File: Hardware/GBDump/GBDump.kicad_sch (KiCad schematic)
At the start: 5 parts, among them U2 TXB0108PW, U3 TXB0108PW, U4 TXB0108PW, U5 Cartridge_Bus

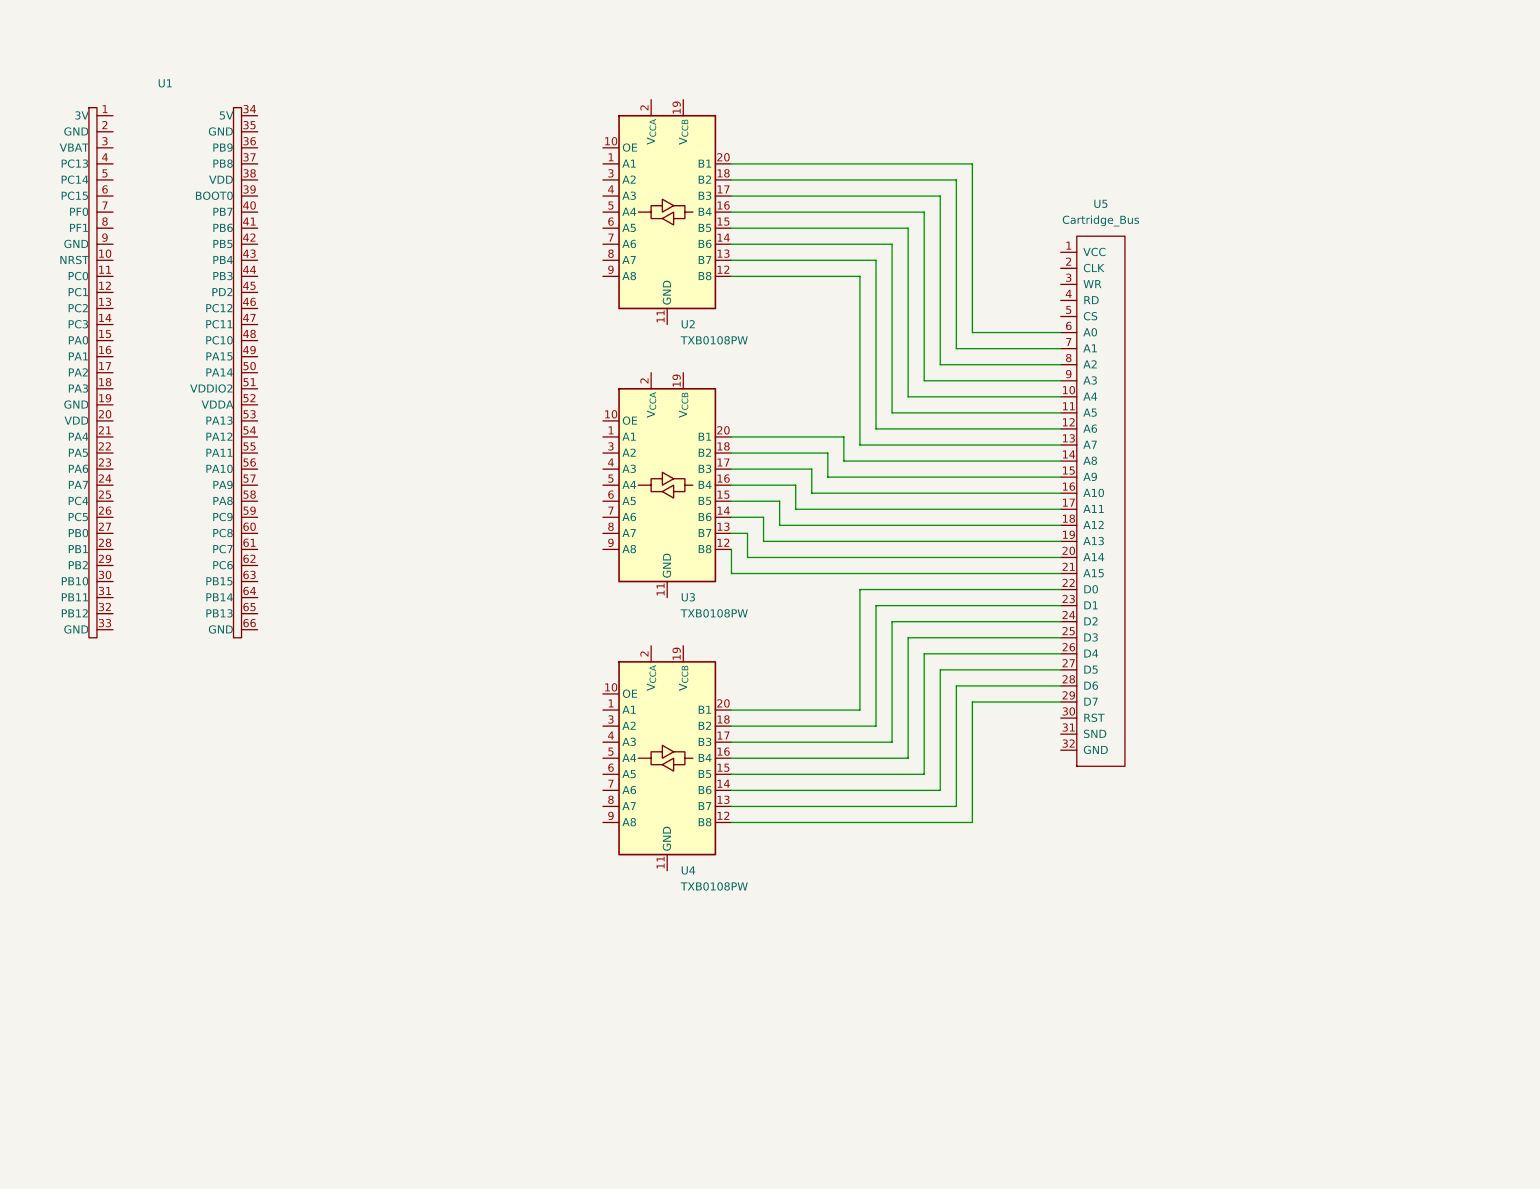
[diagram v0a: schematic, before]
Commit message: Finished address and data bus, level shifting power and ground, jumper for voltage selection.
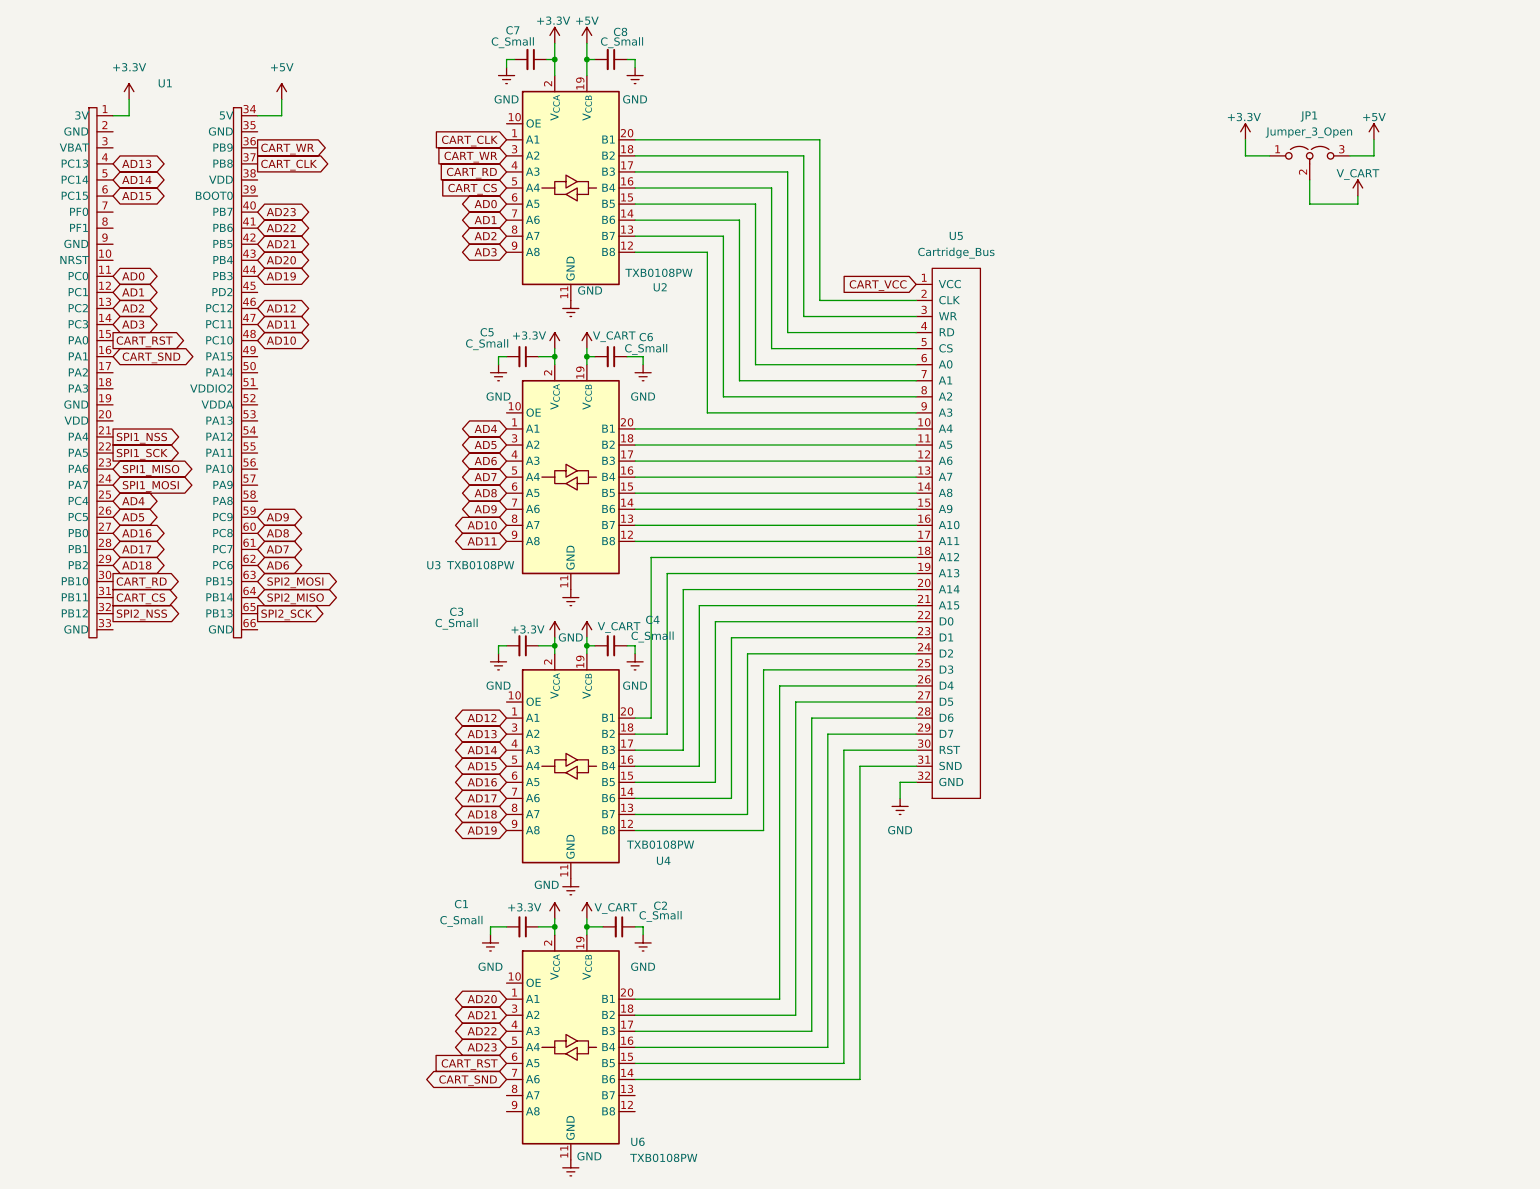
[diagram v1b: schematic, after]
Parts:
- added C1, C2, C3, C4, C5, C6, C7, C8: C_Small, symbol Device:C_Small
- added JP1: Jumper_3_Open, symbol Jumper:Jumper_3_Open
- added U6: TXB0108PW, Package_SO:TSSOP-20_4.4x6.5mm_P0.65mm, symbol Logic_LevelTranslator:TXB0108PW
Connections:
- net AD4: now reaches U3.1 (A1)
- net AD4: now also U1.25 (PC4)
- net GND: now reaches U3.11 (GND)
- net GND: now also U2.11 (GND), U4.11 (GND), U5.32 (GND), C1.2, C2.1, C3.2, C4.1, C5.2, C6.1, C7.2, C8.1, U6.11 (GND)
- net at U3.12 (B8): now also U5.17 (A11); no longer U5.21 (A15)
- net at U3.13 (B7): now also U5.16 (A10); no longer U5.20 (A14)
- net at U3.14 (B6): now also U5.15 (A9); no longer U5.19 (A13)
- net at U3.15 (B5): now also U5.14 (A8); no longer U5.18 (A12)
- net at U3.16 (B4): now also U5.13 (A7); no longer U5.17 (A11)
- net at U3.17 (B3): now also U5.12 (A6); no longer U5.16 (A10)
- net at U3.18 (B2): now also U5.11 (A5); no longer U5.15 (A9)
- net V_CART: now reaches U3.19 (V_{CCB})
- net V_CART: now also U4.19 (V_{CCB}), C2.2, C4.2, C6.2, JP1.2 (C), U6.19 (V_{CCB})
- net +3.3V: now reaches U3.2 (V_{CCA})
- net +3.3V: now also U1.1 (3V), U2.2 (V_{CCA}), U4.2 (V_{CCA}), C1.1, C3.1, C5.1, C7.1, JP1.1 (A), U6.2 (V_{CCA})
- net at U3.20 (B1): now also U5.10 (A4); no longer U5.14 (A8)
- net AD5: now reaches U3.3 (A2)
- net AD5: now also U1.26 (PC5)
- net AD6: now reaches U3.4 (A3)
- net AD6: now also U1.62 (PC6)
- net AD7: now reaches U3.5 (A4)
- net AD7: now also U1.61 (PC7)
- net AD8: now reaches U3.6 (A5)
- net AD8: now also U1.60 (PC8)
- net AD9: now reaches U3.7 (A6)
- net AD9: now also U1.59 (PC9)
- net AD10: now reaches U3.8 (A7)
- net AD10: now also U1.48 (PC10)
- net AD11: now reaches U3.9 (A8)
- net AD11: now also U1.47 (PC11)
- net CART_VCC: now reaches U5.1 (VCC)
- net at U2.15 (B5): now also U5.6 (A0); no longer U5.10 (A4)
- net at U2.14 (B6): now also U5.7 (A1); no longer U5.11 (A5)
- net at U2.13 (B7): now also U5.8 (A2); no longer U5.12 (A6)
- net at U2.12 (B8): now also U5.9 (A3); no longer U5.13 (A7)
- net at U5.2 (CLK~{}): now also U2.20 (B1)
- net at U4.20 (B1): now also U5.18 (A12); no longer U5.22 (D0)
- net at U4.18 (B2): now also U5.19 (A13); no longer U5.23 (D1)
- net at U4.17 (B3): now also U5.20 (A14); no longer U5.24 (D2)
- net at U4.16 (B4): now also U5.21 (A15); no longer U5.25 (D3)
- net at U5.26 (D4): now also U6.20 (B1); no longer U4.15 (B5)
- net at U5.27 (D5): now also U6.18 (B2); no longer U4.14 (B6)
- net at U5.28 (D6): now also U6.17 (B3); no longer U4.13 (B7)
- net at U5.29 (D7): now also U6.16 (B4); no longer U4.12 (B8)
- net at U5.3 (WR): now also U2.18 (B2)
- net at U5.30 (RST): now also U6.15 (B5)
- net at U5.31 (SND): now also U6.14 (B6)
- net at U5.4 (RD): now also U2.17 (B3)
- net at U5.5 (CS): now also U2.16 (B4)
- net CART_CLK: now reaches U2.1 (A1)
- net CART_CLK: now also U1.37 (PB8)
- net +5V: now reaches U2.19 (V_{CCB})
- net +5V: now also U1.34 (5V), C8.2, JP1.3 (B)
- net CART_WR: now reaches U2.3 (A2)
- net CART_WR: now also U1.36 (PB9)
- net CART_RD: now reaches U2.4 (A3)
- net CART_RD: now also U1.30 (PB10)
- net CART_CS: now reaches U2.5 (A4)
- net CART_CS: now also U1.31 (PB11)
- net AD0: now reaches U2.6 (A5)
- net AD0: now also U1.11 (PC0)
- net AD1: now reaches U2.7 (A6)
- net AD1: now also U1.12 (PC1)
- net AD2: now reaches U2.8 (A7)
- net AD2: now also U1.13 (PC2)
- net AD3: now reaches U2.9 (A8)
- net AD3: now also U1.14 (PC3)
- net CART_RST: now reaches U1.15 (PA0)
- net CART_RST: now also U6.6 (A5)
- net CART_SND: now reaches U1.16 (PA1)
- net CART_SND: now also U6.7 (A6)
- net SPI1_NSS: now reaches U1.21 (PA4)
- net SPI1_SCK: now reaches U1.22 (PA5)
- net SPI1_MISO: now reaches U1.23 (PA6)
- net SPI1_MOSI: now reaches U1.24 (PA7)
- net AD16: now reaches U1.27 (PB0)
- net AD16: now also U4.6 (A5)
- net AD17: now reaches U1.28 (PB1)
- net AD17: now also U4.7 (A6)
- net AD18: now reaches U1.29 (PB2)
- net AD18: now also U4.8 (A7)
- net SPI2_NSS: now reaches U1.32 (PB12)
- net AD13: now reaches U1.4 (PC13)
- net AD13: now also U4.3 (A2)
- net AD23: now reaches U1.40 (PB7)
- net AD23: now also U6.5 (A4)
- net AD22: now reaches U1.41 (PB6)
- net AD22: now also U6.4 (A3)
- net AD21: now reaches U1.42 (PB5)
- net AD21: now also U6.3 (A2)
- net AD20: now reaches U1.43 (PB4)
- net AD20: now also U6.1 (A1)
- net AD19: now reaches U1.44 (PB3)
- net AD19: now also U4.9 (A8)
- net AD12: now reaches U1.46 (PC12)
- net AD12: now also U4.1 (A1)
- net AD14: now reaches U1.5 (PC14)
- net AD14: now also U4.4 (A3)
- net AD15: now reaches U1.6 (PC15)
- net AD15: now also U4.5 (A4)
- net SPI2_MOSI: now reaches U1.63 (PB15)
- net SPI2_MISO: now reaches U1.64 (PB14)
- net SPI2_SCK: now reaches U1.65 (PB13)
- new net: U4.15 (B5), U5.22 (D0)
- new net: U4.14 (B6), U5.23 (D1)
- new net: U4.13 (B7), U5.24 (D2)
- new net: U4.12 (B8), U5.25 (D3)
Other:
- moved on the sheet: U2, U3, U4, U5

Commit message: Added SPI header, symbol files
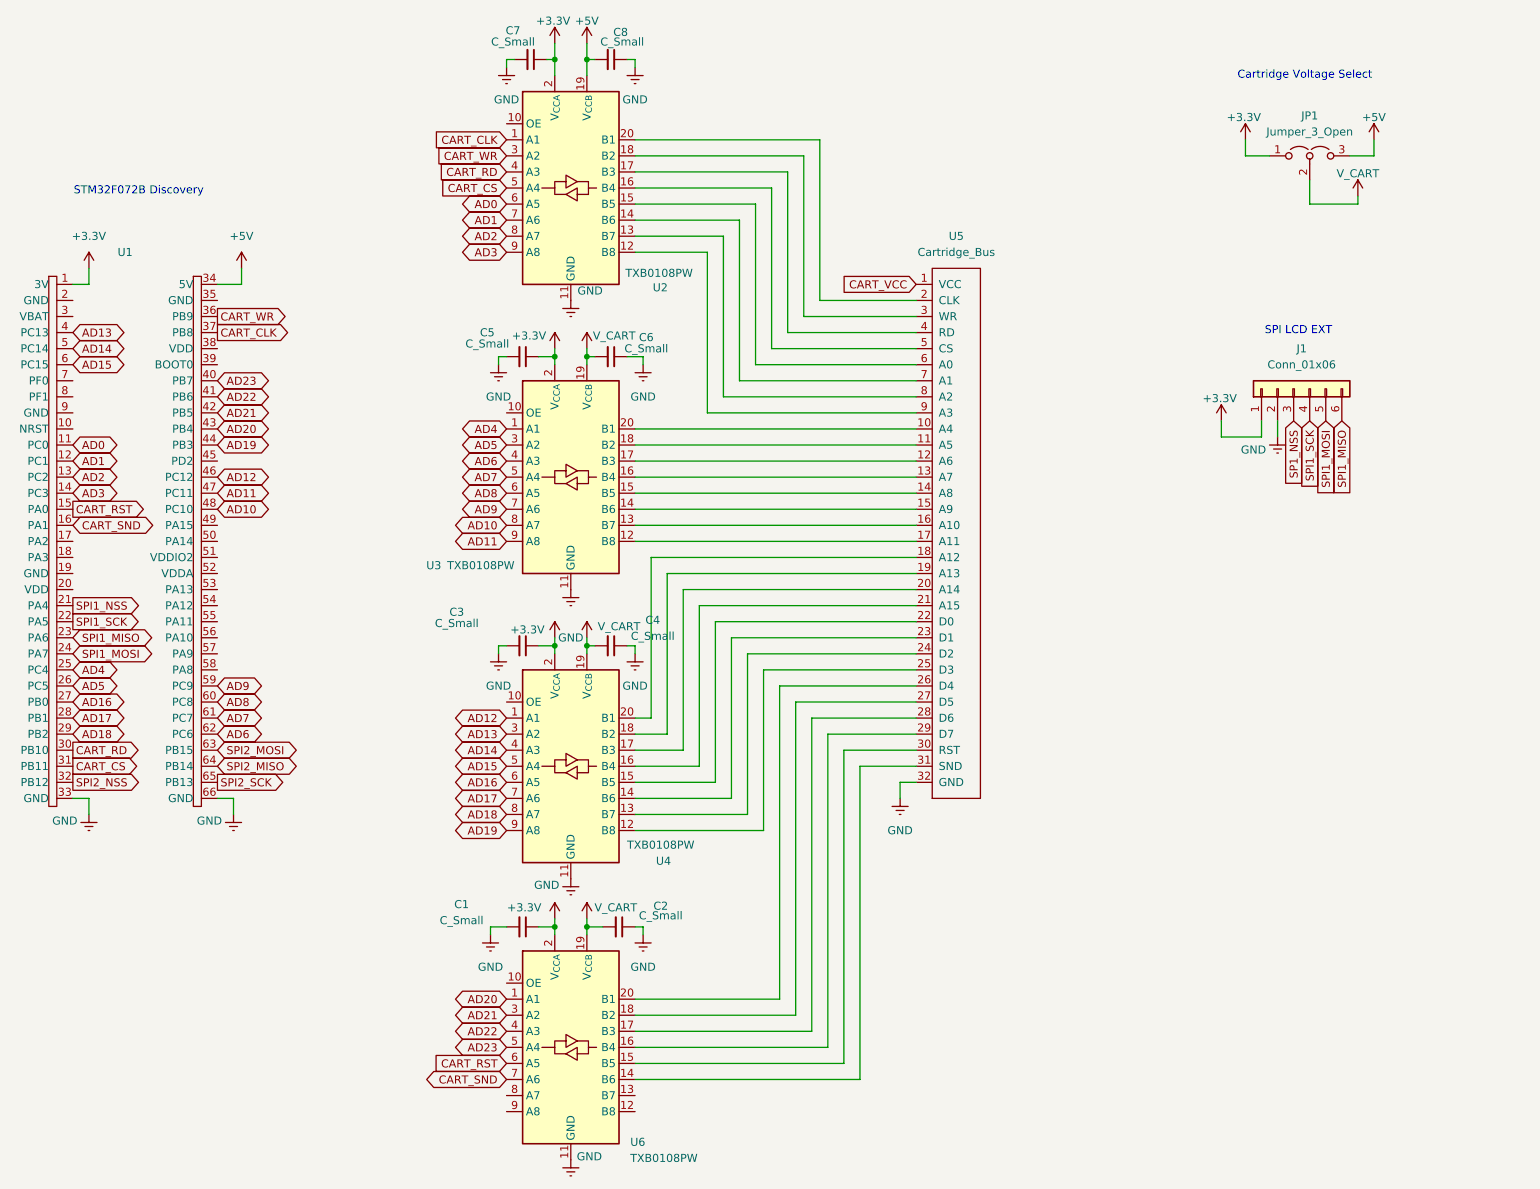
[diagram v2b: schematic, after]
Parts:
- added J1: Conn_01x06, symbol GBADump_Library:Conn_01x06
- C1, C2, C3, C4, C5, C6, C7, C8: symbol Device:C_Small -> GBADump_Library:C_Small
- JP1: symbol Jumper:Jumper_3_Open -> GBADump_Library:Jumper_3_Open
- U1: symbol Connector:STM32F072B-DISCO -> GBADump_Library:STM32F072B-DISCO
- U2, U3, U4, U6: symbol Logic_LevelTranslator:TXB0108PW -> GBADump_Library:TXB0108PW
- U5: symbol HDR_Gameboy:Cartridge_Bus -> GBADump_Library:Cartridge_Bus
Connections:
- net +3.3V: now also J1.1 (Pin_1)
- net GND: now also U1.33 (GND), U1.66 (GND), J1.2 (Pin_2)
- net SPI1_MISO: now also J1.6 (Pin_6)
- net SPI1_MOSI: now also J1.5 (Pin_5)
- net SPI1_SCK: now also J1.4 (Pin_4)
- new net SP1_NSS: J1.3 (Pin_3)
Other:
- note added: "Cartridge Voltage Select"
- note added: "SPI LCD EXT"
- note added: "STM32F072B Discovery"
- moved on the sheet: U1

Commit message: Added SD interface and level shift enable pin with pull down
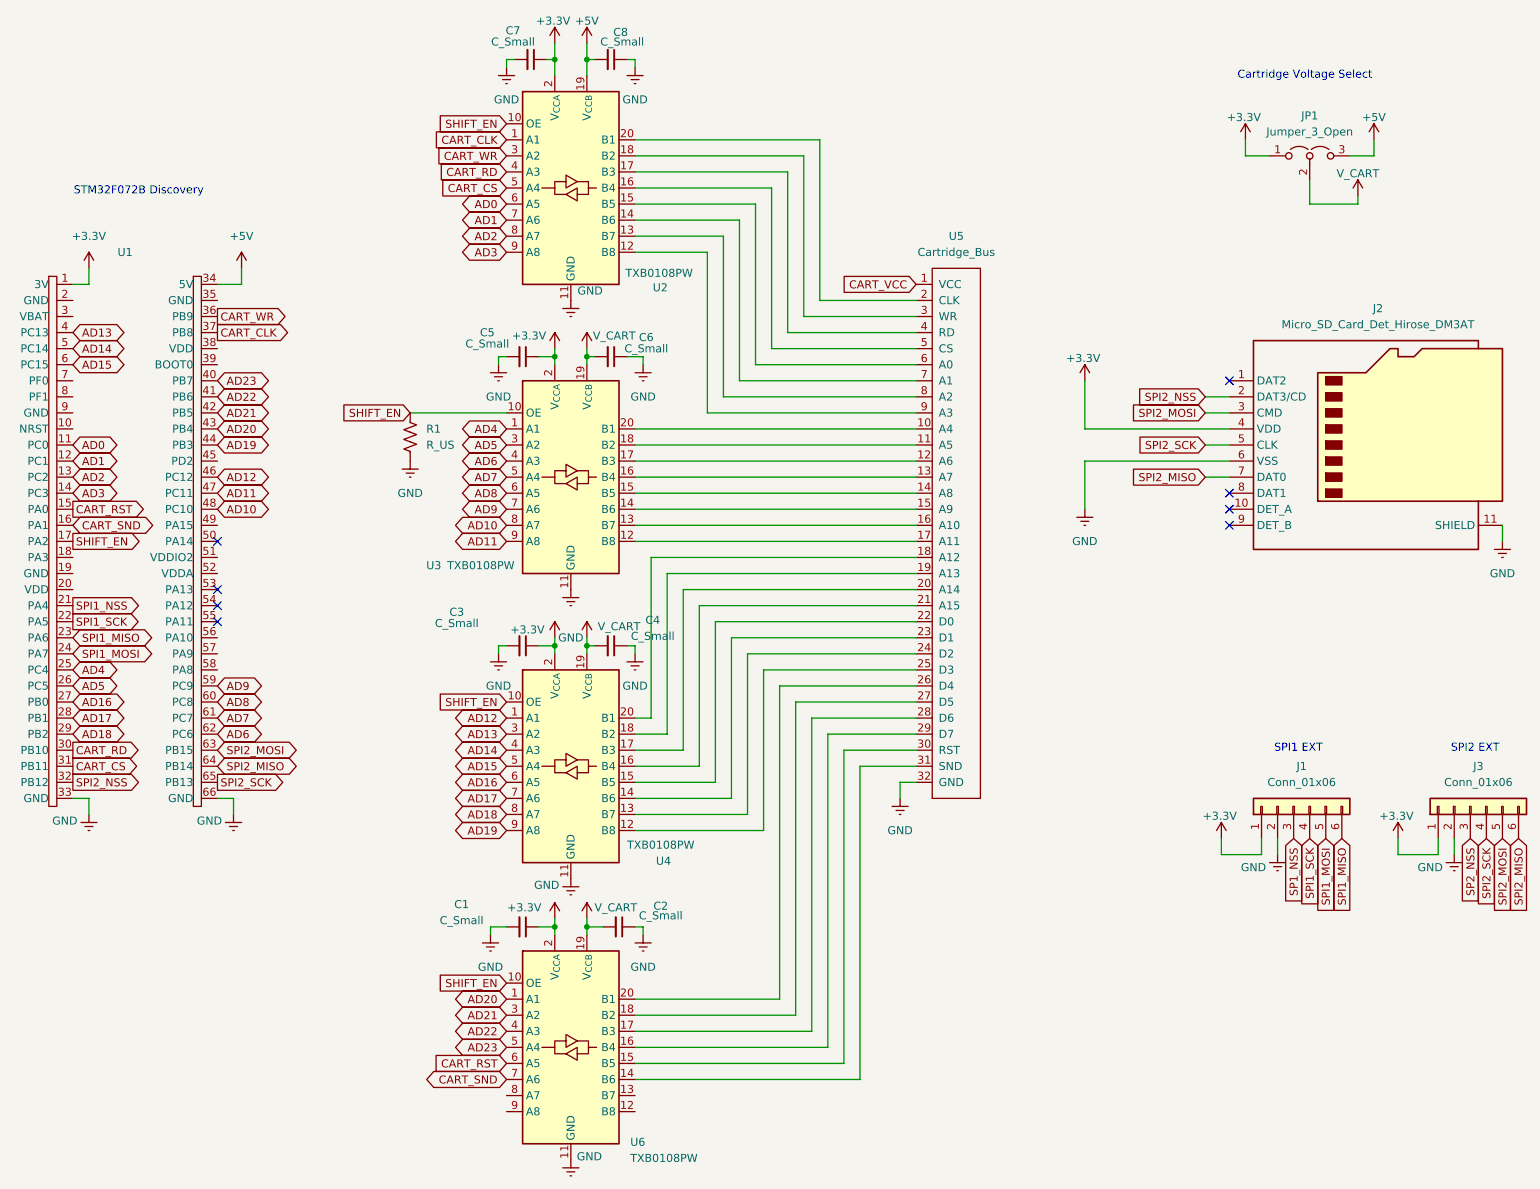
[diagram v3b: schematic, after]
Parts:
- added J2: Micro_SD_Card_Det_Hirose_DM3AT, symbol GBADump_Library:Micro_SD_Card_Det_Hirose_DM3AT
- added J3: Conn_01x06, symbol GBADump_Library:Conn_01x06
- added R1: R_US, symbol GBADump_Library:R_US
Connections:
- net +3.3V: now also J2.4 (VDD), J3.1 (Pin_1)
- net GND: now also J2.11 (SHIELD), J2.6 (VSS), J3.2 (Pin_2), R1.2
- net SPI2_MISO: now also J2.7 (DAT0), J3.6 (Pin_6)
- net SPI2_MOSI: now also J2.3 (CMD), J3.5 (Pin_5)
- net SPI2_NSS: now also J2.2 (DAT3/CD)
- net SPI2_SCK: now also J2.5 (CLK), J3.4 (Pin_4)
- net SHIFT_EN: now reaches U6.10 (OE)
- net SHIFT_EN: now also U1.17 (PA2), U2.10 (OE), U3.10 (OE), U4.10 (OE), R1.1
- new net SP2_NSS: J3.3 (Pin_3)
- no-connect marks 0 -> 8
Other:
- note added: "SPI1 EXT"
- note added: "SPI2 EXT"
- note removed: "SPI LCD EXT"
- moved on the sheet: J1
